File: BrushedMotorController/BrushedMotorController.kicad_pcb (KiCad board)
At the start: 2 copper layers, 35.3 x 64.1 mm, 33 parts, among them Q1 SI4156DY, Q2 SI4156DY, Q3 SI4156DY, Q4 SI4156DY, U1 74LVC2G04, U2 IRS2005S, U3 IRS2005S, U4 74HC00

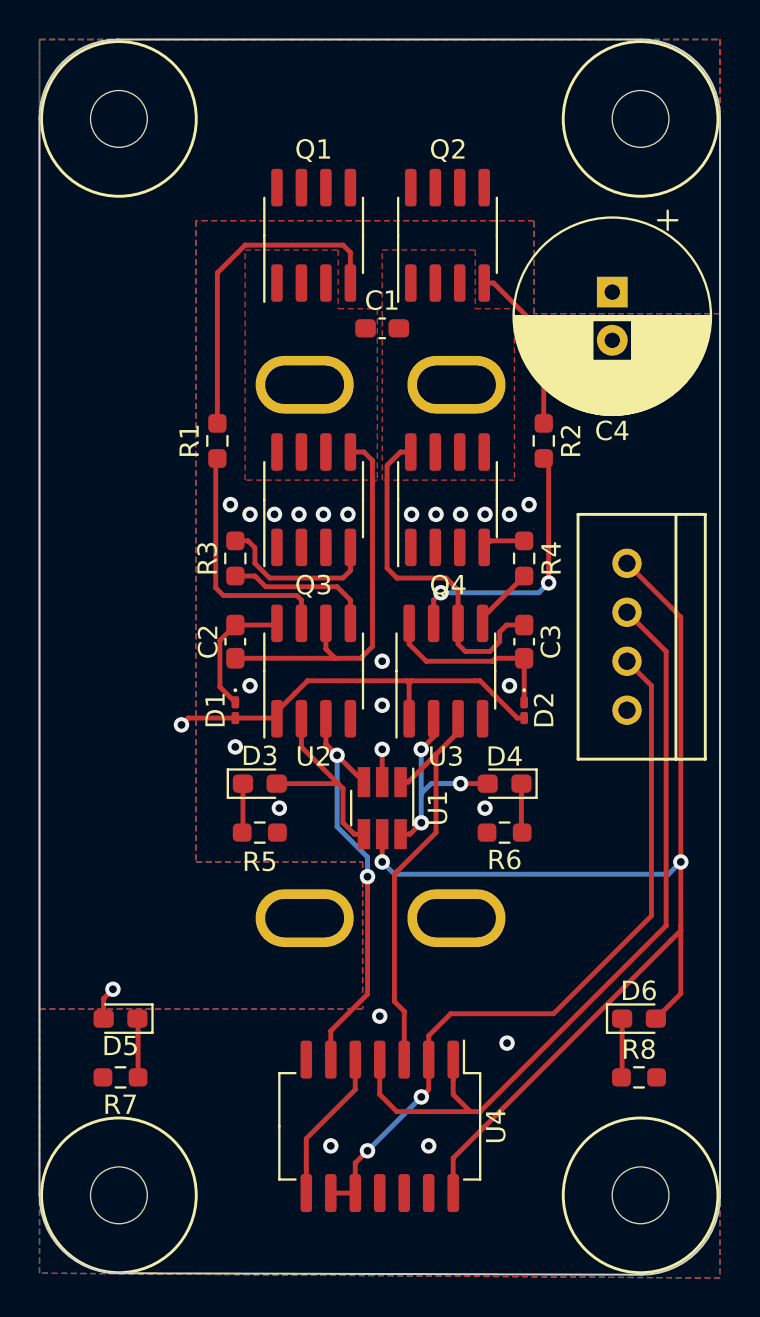
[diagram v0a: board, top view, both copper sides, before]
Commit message: Switch to 4-layer
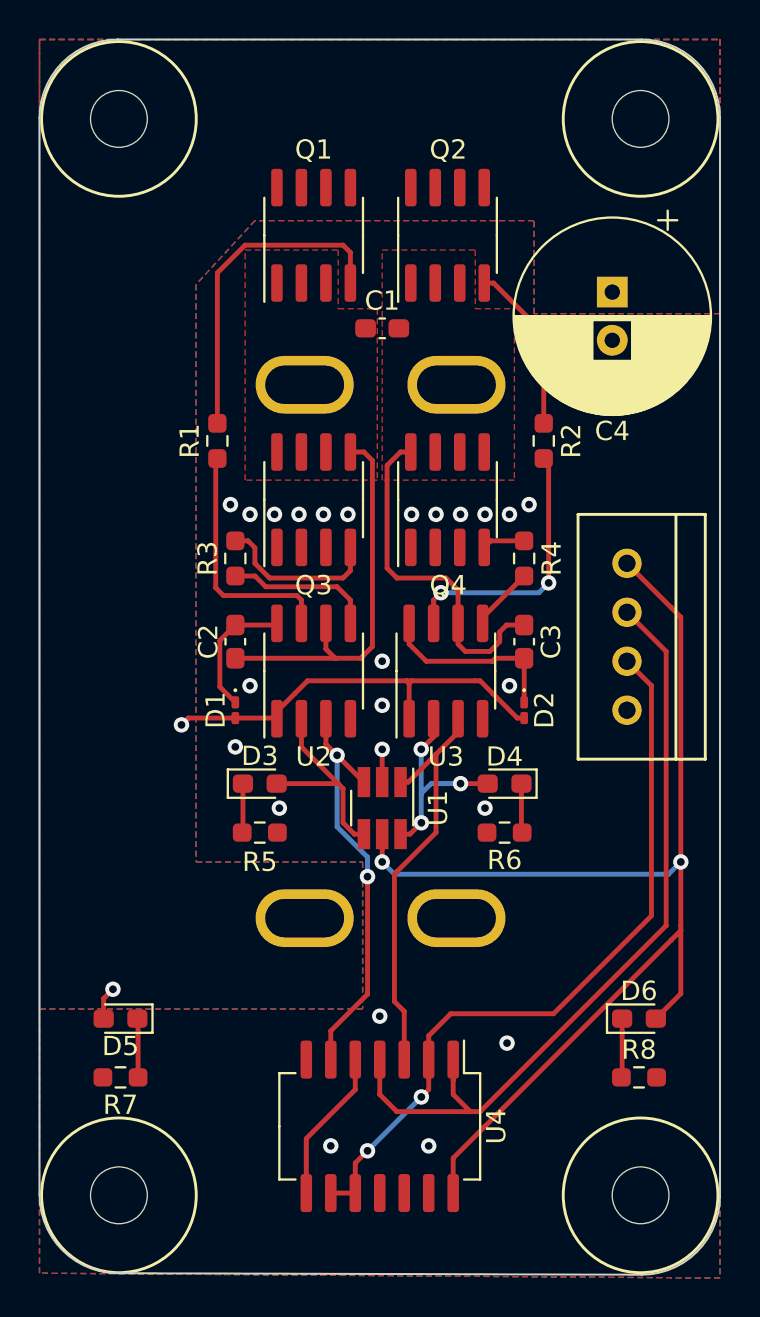
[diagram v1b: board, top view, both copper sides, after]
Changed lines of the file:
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@@
         (xy 182.626 67.056)
         (xy 182.626 62.23)
-        (xy 165.1 62.23)
+        (xy 168.148 62.23)
+        (xy 165.1 65.532)
         (xy 165.1 95.504)
         (xy 173.736 95.504)
